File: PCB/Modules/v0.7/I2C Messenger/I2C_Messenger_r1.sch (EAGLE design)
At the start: 21 parts, among them IC1 SN65HVD31DR, IC2 PCA9517

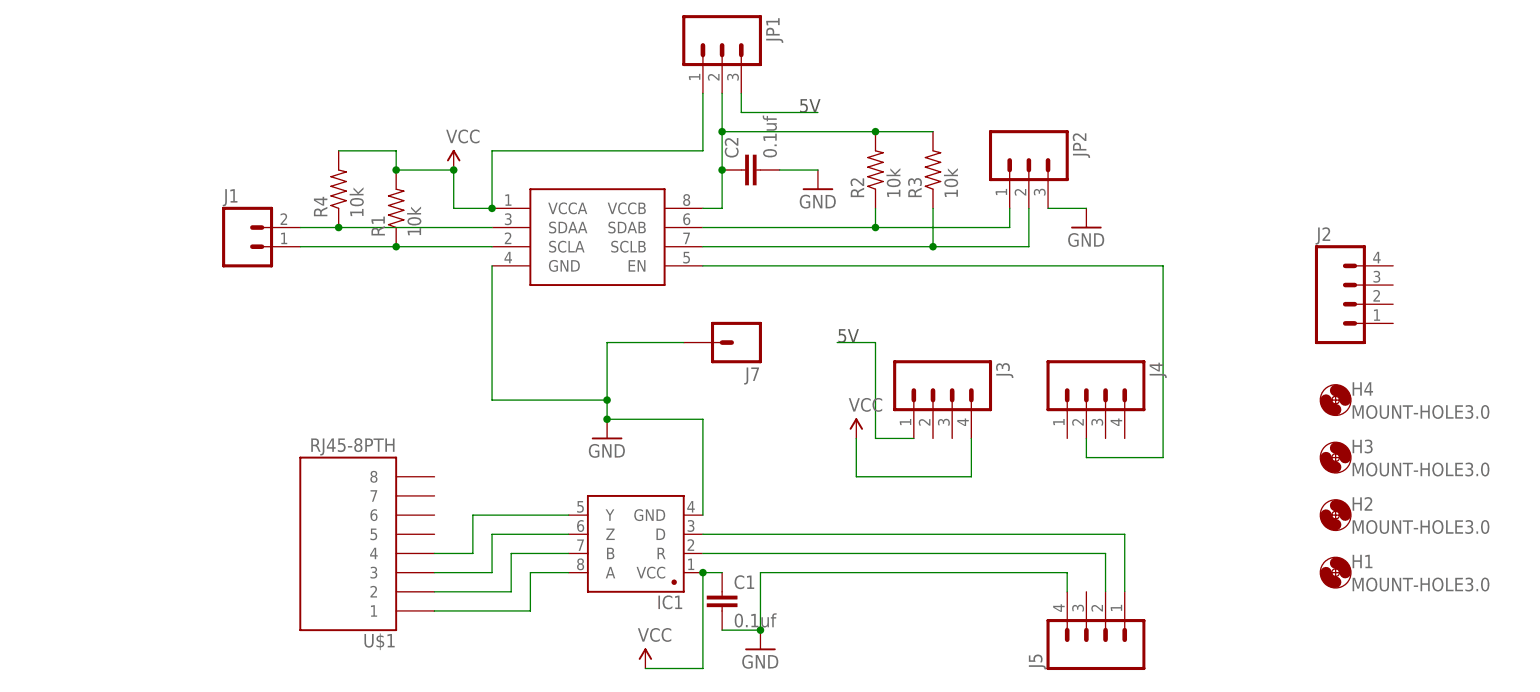
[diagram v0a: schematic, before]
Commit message: - Added 8-channel analog output PCB - Updated I2C module PCB - Reorganized repository to put PCB bottom insulator designs in 1 folder -
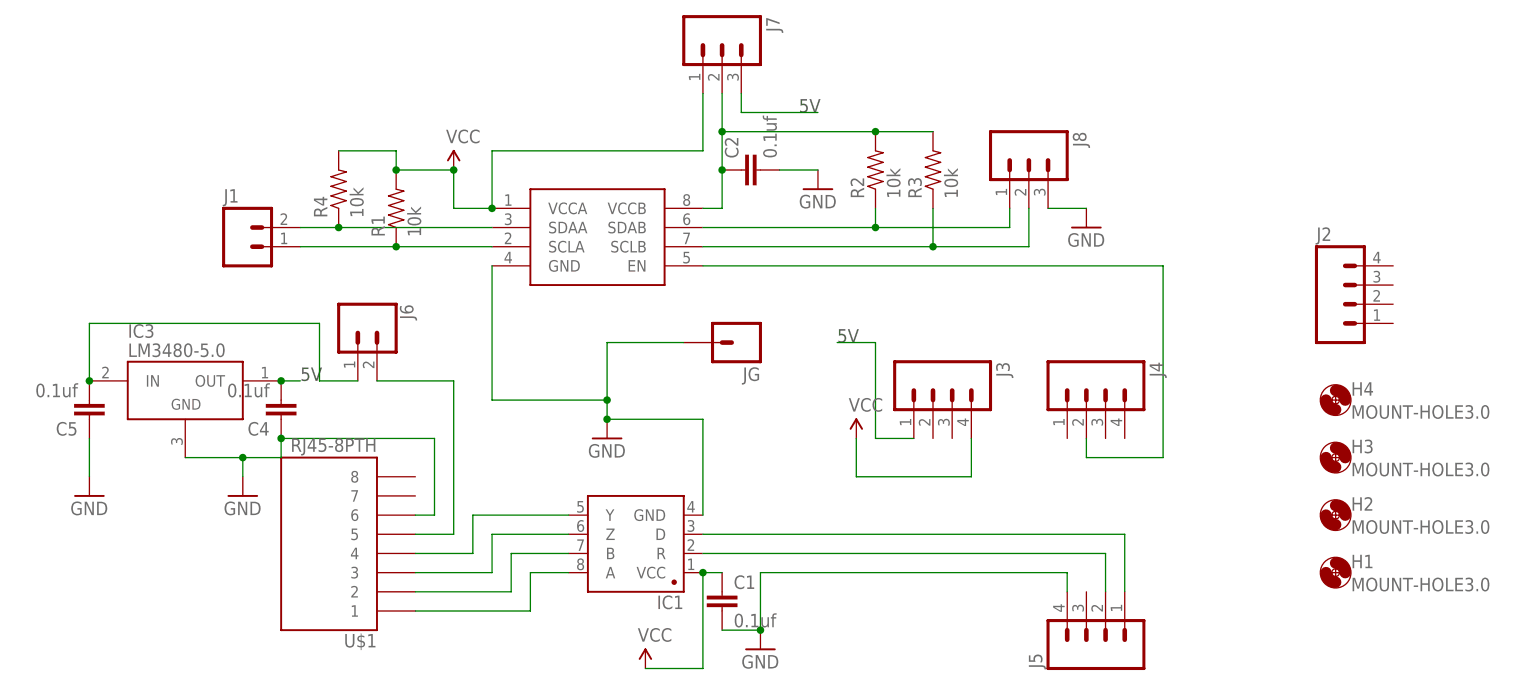
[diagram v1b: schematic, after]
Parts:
- removed JP1: (no value), SparkFun-Connectors:M03PTH
- added C4, C5: 0.1uf, SparkFun-Capacitors:CAP1206
- added IC3: LM3480-5.0, regulators:LM3480-5.0
- added J6: (no value), SparkFun-Connectors:CONN_02
- added JG: (no value), SparkFun-Connectors:M01PTH
- J7: device SparkFun-Connectors:M01PTH -> SparkFun-Connectors:M03PTH
- renumbered JP2 to J8
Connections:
- new net N$1: J6.2, U$1.5
- new net N$26: C5.2, IC3.IN, J6.1
- net 5V: now also C4.2, IC3.OUT, J7.3; no longer JP1.3
- net GND: now also C4.1, C5.1, IC3.GND, JG.1, U$1.6; no longer J7.1
- net N$12: now also J7.2; no longer JP1.2
- net VCC: now also J7.1; no longer JP1.1
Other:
- moved on the sheet: U$1
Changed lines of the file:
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@@
 <?xml version="1.0" encoding="utf-8"?>
 <!DOCTYPE eagle SYSTEM "eagle.dtd">
-<eagle version="6.3">
+<eagle version="7.7.0">
 <drawing>
 <settings>
@@
 <part name="C2" library="SparkFun-Capacitors" deviceset="CAP" device="1206" value="0.1uf"/>
 <part name="GND4" library="SparkFun-Aesthetics" deviceset="GND" device=""/>
-<part name="JP1" library="SparkFun-Connectors" deviceset="M03" device="PTH"/>
+<part name="J7" library="SparkFun-Connectors" deviceset="M03" device="PTH"/>
 <part name="R2" library="SparkFun-Resistors" deviceset="RESISTOR" device="1206" value="10k"/>
 <part name="R3" library="SparkFun-Resistors" deviceset="RESISTOR" device="1206" value="10k"/>
-<part name="JP2" library="SparkFun-Connectors" deviceset="M03" device="SCREW_LOCK"/>
+<part name="J8" library="SparkFun-Connectors" deviceset="M03" device="SCREW_LOCK"/>
 <part name="GND5" library="SparkFun-Aesthetics" deviceset="GND" device=""/>
-<part name="J7" library="SparkFun-Connectors" deviceset="M01" device="PTH"/>
+<part name="JG" library="SparkFun-Connectors" deviceset="M01" device="PTH"/>
 <part name="J5" library="SparkFun-Connectors" deviceset="M04" device="PTH"/>
 <part name="H1" library="holes" deviceset="MOUNT-HOLE" device="3.0"/>
@@
 <part name="R1" library="SparkFun-Resistors" deviceset="RESISTOR" device="1206" value="10k"/>
 <part name="R4" library="SparkFun-Resistors" deviceset="RESISTOR" device="1206" value="10k"/>
+<part name="IC3" library="regulators" deviceset="LM3480-*" device="" technology="5.0"/>
+<part name="C4" library="SparkFun-Capacitors" deviceset="CAP" device="1206" value="0.1uf"/>
+<part name="C5" library="SparkFun-Capacitors" deviceset="CAP" device="1206" value="0.1uf"/>
+<part name="GND2" library="SparkFun-Aesthetics" deviceset="GND" device=""/>
+<part name="GND6" library="SparkFun-Aesthetics" deviceset="GND" device=""/>
+<part name="J6" library="SparkFun-Connectors" deviceset="CONN_02" device=""/>
 </parts>
 <sheets>
@@
 <text x="124.46" y="68.58" size="1.778" layer="97">5V</text>
 <text x="119.38" y="99.06" size="1.778" layer="97">5V</text>
+<text x="53.34" y="63.5" size="1.778" layer="97">5V</text>
 </plain>
 <instances>
-<instance part="U$1" gate="G$1" x="58.42" y="43.18" rot="R180"/>
+<instance part="U$1" gate="G$1" x="55.88" y="43.18" rot="R180"/>
 <instance part="GND1" gate="1" x="93.98" y="55.88"/>
 <instance part="IC1" gate="G$1" x="104.14" y="38.1" rot="R180"/>
@@
 <instance part="C2" gate="G$1" x="114.3" y="91.44" rot="R90"/>
 <instance part="GND4" gate="1" x="121.92" y="88.9"/>
-<instance part="JP1" gate="G$1" x="109.22" y="109.22" rot="R270"/>
+<instance part="J7" gate="G$1" x="109.22" y="109.22" rot="R270"/>
 <instance part="R2" gate="G$1" x="129.54" y="91.44" rot="R90"/>
 <instance part="R3" gate="G$1" x="137.16" y="91.44" rot="R90"/>
-<instance part="JP2" gate="G$1" x="149.86" y="93.98" rot="R270"/>
+<instance part="J8" gate="G$1" x="149.86" y="93.98" rot="R270"/>
 <instance part="GND5" gate="1" x="157.48" y="83.82"/>
-<instance part="J7" gate="G$1" x="111.76" y="68.58" rot="R180"/>
+<instance part="JG" gate="G$1" x="111.76" y="68.58" rot="R180"/>
 <instance part="J5" gate="G$1" x="160.02" y="30.48" rot="R90"/>
 <instance part="H1" gate="G$1" x="190.5" y="38.1"/>
@@
 <instance part="R1" gate="G$1" x="66.04" y="86.36" rot="R90"/>
 <instance part="R4" gate="G$1" x="58.42" y="88.9" rot="R90"/>
+<instance part="IC3" gate="G$1" x="38.1" y="63.5"/>
+<instance part="C4" gate="G$1" x="50.8" y="60.96" rot="R180"/>
+<instance part="C5" gate="G$1" x="25.4" y="60.96" rot="R180"/>
+<instance part="GND2" gate="1" x="25.4" y="48.26"/>
+<instance part="GND6" gate="1" x="45.72" y="48.26"/>
+<instance part="J6" gate="G$1" x="60.96" y="71.12" rot="R270"/>
 </instances>
 <busses>
@@
 <wire x1="93.98" y1="60.96" x2="93.98" y2="68.58" width="0.1524" layer="91"/>
 <junction x="93.98" y="60.96"/>
-<pinref part="J7" gate="G$1" pin="1"/>
+<pinref part="JG" gate="G$1" pin="1"/>
 <wire x1="93.98" y1="68.58" x2="104.14" y2="68.58" width="0.1524" layer="91"/>
 </segment>
@@
 </segment>
 <segment>
-<pinref part="JP2" gate="G$1" pin="3"/>
+<pinref part="J8" gate="G$1" pin="3"/>
 <pinref part="GND5" gate="1" pin="GND"/>
 <wire x1="152.4" y1="86.36" x2="157.48" y2="86.36" width="0.1524" layer="91"/>
+</segment>
+<segment>
+<pinref part="GND2" gate="1" pin="GND"/>
+<pinref part="C5" gate="G$1" pin="1"/>
+<wire x1="25.4" y1="50.8" x2="25.4" y2="55.88" width="0.1524" layer="91"/>
+</segment>
+<segment>
+<pinref part="IC3" gate="G$1" pin="GND"/>
+<pinref part="GND6" gate="1" pin="GND"/>
+<wire x1="38.1" y1="53.34" x2="45.72" y2="53.34" width="0.1524" layer="91"/>
+<wire x1="45.72" y1="53.34" x2="45.72" y2="50.8" width="0.1524" layer="91"/>
+<pinref part="C4" gate="G$1" pin="1"/>
+<wire x1="45.72" y1="53.34" x2="50.8" y2="53.34" width="0.1524" layer="91"/>
+<wire x1="50.8" y1="53.34" x2="50.8" y2="55.88" width="0.1524" layer="91"/>
+<junction x="45.72" y="53.34"/>
+<pinref part="U$1" gate="G$1" pin="6"/>
+<wire x1="68.58" y1="45.72" x2="71.12" y2="45.72" width="0.1524" layer="91"/>
+<wire x1="71.12" y1="45.72" x2="71.12" y2="55.88" width="0.1524" layer="91"/>
+<wire x1="71.12" y1="55.88" x2="50.8" y2="55.88" width="0.1524" layer="91"/>
+<junction x="50.8" y="55.88"/>
 </segment>
 </net>
@@
 <wire x1="83.82" y1="38.1" x2="83.82" y2="33.02" width="0.1524" layer="91"/>
 <pinref part="U$1" gate="G$1" pin="1"/>
-<wire x1="83.82" y1="33.02" x2="71.12" y2="33.02" width="0.1524" layer="91"/>
+<wire x1="83.82" y1="33.02" x2="68.58" y2="33.02" width="0.1524" layer="91"/>
 </segment>
 </net>
@@
 <segment>
 <pinref part="U$1" gate="G$1" pin="2"/>
-<wire x1="71.12" y1="35.56" x2="81.28" y2="35.56" width="0.1524" layer="91"/>
+<wire x1="68.58" y1="35.56" x2="81.28" y2="35.56" width="0.1524" layer="91"/>
 <wire x1="81.28" y1="35.56" x2="81.28" y2="40.64" width="0.1524" layer="91"/>
 <pinref part="IC1" gate="G$1" pin="B"/>
@@
 <segment>
 <pinref part="U$1" gate="G$1" pin="3"/>
-<wire x1="71.12" y1="38.1" x2="78.74" y2="38.1" width="0.1524" layer="91"/>
+<wire x1="68.58" y1="38.1" x2="78.74" y2="38.1" width="0.1524" layer="91"/>
 <wire x1="78.74" y1="38.1" x2="78.74" y2="43.18" width="0.1524" layer="91"/>
 <pinref part="IC1" gate="G$1" pin="Z"/>
@@
 <segment>
 <pinref part="U$1" gate="G$1" pin="4"/>
-<wire x1="71.12" y1="40.64" x2="76.2" y2="40.64" width="0.1524" layer="91"/>
+<wire x1="68.58" y1="40.64" x2="76.2" y2="40.64" width="0.1524" layer="91"/>
 <wire x1="76.2" y1="40.64" x2="76.2" y2="45.72" width="0.1524" layer="91"/>
 <pinref part="IC1" gate="G$1" pin="Y"/>
@@
 <wire x1="78.74" y1="86.36" x2="73.66" y2="86.36" width="0.1524" layer="91"/>
 <wire x1="73.66" y1="86.36" x2="73.66" y2="91.44" width="0.1524" layer="91"/>
-<pinref part="JP1" gate="G$1" pin="1"/>
+<pinref part="J7" gate="G$1" pin="1"/>
 <wire x1="106.68" y1="101.6" x2="106.68" y2="93.98" width="0.1524" layer="91"/>
 <wire x1="106.68" y1="93.98" x2="78.74" y2="93.98" width="0.1524" layer="91"/>
@@
 </segment>
 <segment>
-<pinref part="JP1" gate="G$1" pin="3"/>
+<pinref part="J7" gate="G$1" pin="3"/>
 <wire x1="111.76" y1="101.6" x2="111.76" y2="99.06" width="0.1524" layer="91"/>
 <wire x1="111.76" y1="99.06" x2="121.92" y2="99.06" width="0.1524" layer="91"/>
+</segment>
+<segment>
+<pinref part="IC3" gate="G$1" pin="OUT"/>
+<wire x1="50.8" y1="63.5" x2="53.34" y2="63.5" width="0.1524" layer="91"/>
+<pinref part="C4" gate="G$1" pin="2"/>
+<junction x="50.8" y="63.5"/>
 </segment>
 </net>
@@
 <wire x1="137.16" y1="96.52" x2="129.54" y2="96.52" width="0.1524" layer="91"/>
 <pinref part="C2" gate="G$1" pin="1"/>
-<pinref part="JP1" gate="G$1" pin="2"/>
+<pinref part="J7" gate="G$1" pin="2"/>
 <wire x1="109.22" y1="101.6" x2="109.22" y2="96.52" width="0.1524" layer="91"/>
 <wire x1="109.22" y1="96.52" x2="109.22" y2="91.44" width="0.1524" layer="91"/>
@@
 <junction x="129.54" y="83.82"/>
 <wire x1="147.32" y1="83.82" x2="147.32" y2="86.36" width="0.1524" layer="91"/>
-<pinref part="JP2" gate="G$1" pin="1"/>
+<pinref part="J8" gate="G$1" pin="1"/>
 </segment>
 </net>
@@
 <junction x="137.16" y="81.28"/>
 <wire x1="149.86" y1="81.28" x2="149.86" y2="86.36" width="0.1524" layer="91"/>
-<pinref part="JP2" gate="G$1" pin="2"/>
-</segment>
-</net>
+<pinref part="J8" gate="G$1" pin="2"/>
+</segment>
+</net>
+<net name="N$26" class="0">
+<segment>
+<pinref part="IC3" gate="G$1" pin="IN"/>
+<wire x1="25.4" y1="71.12" x2="25.4" y2="63.5" width="0.1524" layer="91"/>
+<pinref part="C5" gate="G$1" pin="2"/>
+<junction x="25.4" y="63.5"/>
+<wire x1="25.4" y1="71.12" x2="55.88" y2="71.12" width="0.1524" layer="91"/>
+<wire x1="55.88" y1="71.12" x2="55.88" y2="63.5" width="0.1524" layer="91"/>
+<pinref part="J6" gate="G$1" pin="1"/>
+<wire x1="55.88" y1="63.5" x2="60.96" y2="63.5" width="0.1524" layer="91"/>
+</segment>
+</net>
+<net name="N$1" class="0">
+<segment>
+<pinref part="U$1" gate="G$1" pin="5"/>
+<wire x1="68.58" y1="43.18" x2="73.66" y2="43.18" width="0.1524" layer="91"/>
+<wire x1="73.66" y1="43.18" x2="73.66" y2="63.5" width="0.1524" layer="91"/>
+<pinref part="J6" gate="G$1" pin="2"/>
+<wire x1="73.66" y1="63.5" x2="63.5" y2="63.5" width="0.1524" layer="91"/>
+</segment>
+</net>
